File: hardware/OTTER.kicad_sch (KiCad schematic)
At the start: 0 parts

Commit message: added eth symbol
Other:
- added sheet Ethernet (Ethernet.kicad_sch)
- title: (none) -> OTTER Board
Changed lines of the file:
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@@
 	(generator_version "10.0")
 	(paper "A4")
+	(title_block
+		(title "OTTER Board")
+		(date "2026-08-11")
+		(rev "A")
+	)
+	(sheet
+		(at 35.56 29.21)
+		(size 85.09 41.91)
+		(exclude_from_sim no)
+		(in_bom yes)
+		(on_board yes)
+		(dnp no)
+		(fields_autoplaced yes)
+		(stroke
+			(width 0.1524)
+			(type solid)
+		)
+		(fill
+			(color 0 0 0 0)
+		)
+		(property "Sheetname" "Ethernet"
+			(at 35.56 28.4984 0)
+			(show_name no)
+			(do_not_autoplace no)
+			(effects
+				(font
+					(size 1.27 1.27)
+				)
+				(justify left bottom)
+			)
+		)
+		(property "Sheetfile" "Ethernet.kicad_sch"
+			(at 35.56 71.7046 0)
+			(show_name no)
+			(do_not_autoplace no)
+			(effects
+				(font
+					(size 1.27 1.27)
+				)
+				(justify left top)
+			)
+		)
+		(instances
+			(project "OTTER"
+				(path "/db2a353b-4a3a-4ce7-8df7-bc33bc3b7cc7"
+					(page "2")
+				)
+			)
+		)
+	)
 	(sheet_instances
 		(path "/"

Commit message: poop
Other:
- added sheet DDRAM (DDRAM.kicad_sch)
- added sheet HDMI (HDMI.kicad_sch)
- added sheet Periphs (Periphs.kicad_sch)
- added sheet Power (Power.kicad_sch)
- added sheet USB (USB.kicad_sch)
- added sheet ZED (ZED.kicad_sch)
- note added: "+ more bs to come"

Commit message: poop
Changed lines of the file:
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@@
 	(text "+ more bs to come"
 		(exclude_from_sim no)
-		(at 105.664 151.384 0)
+		(at 148.844 154.178 0)
 		(effects
 			(font

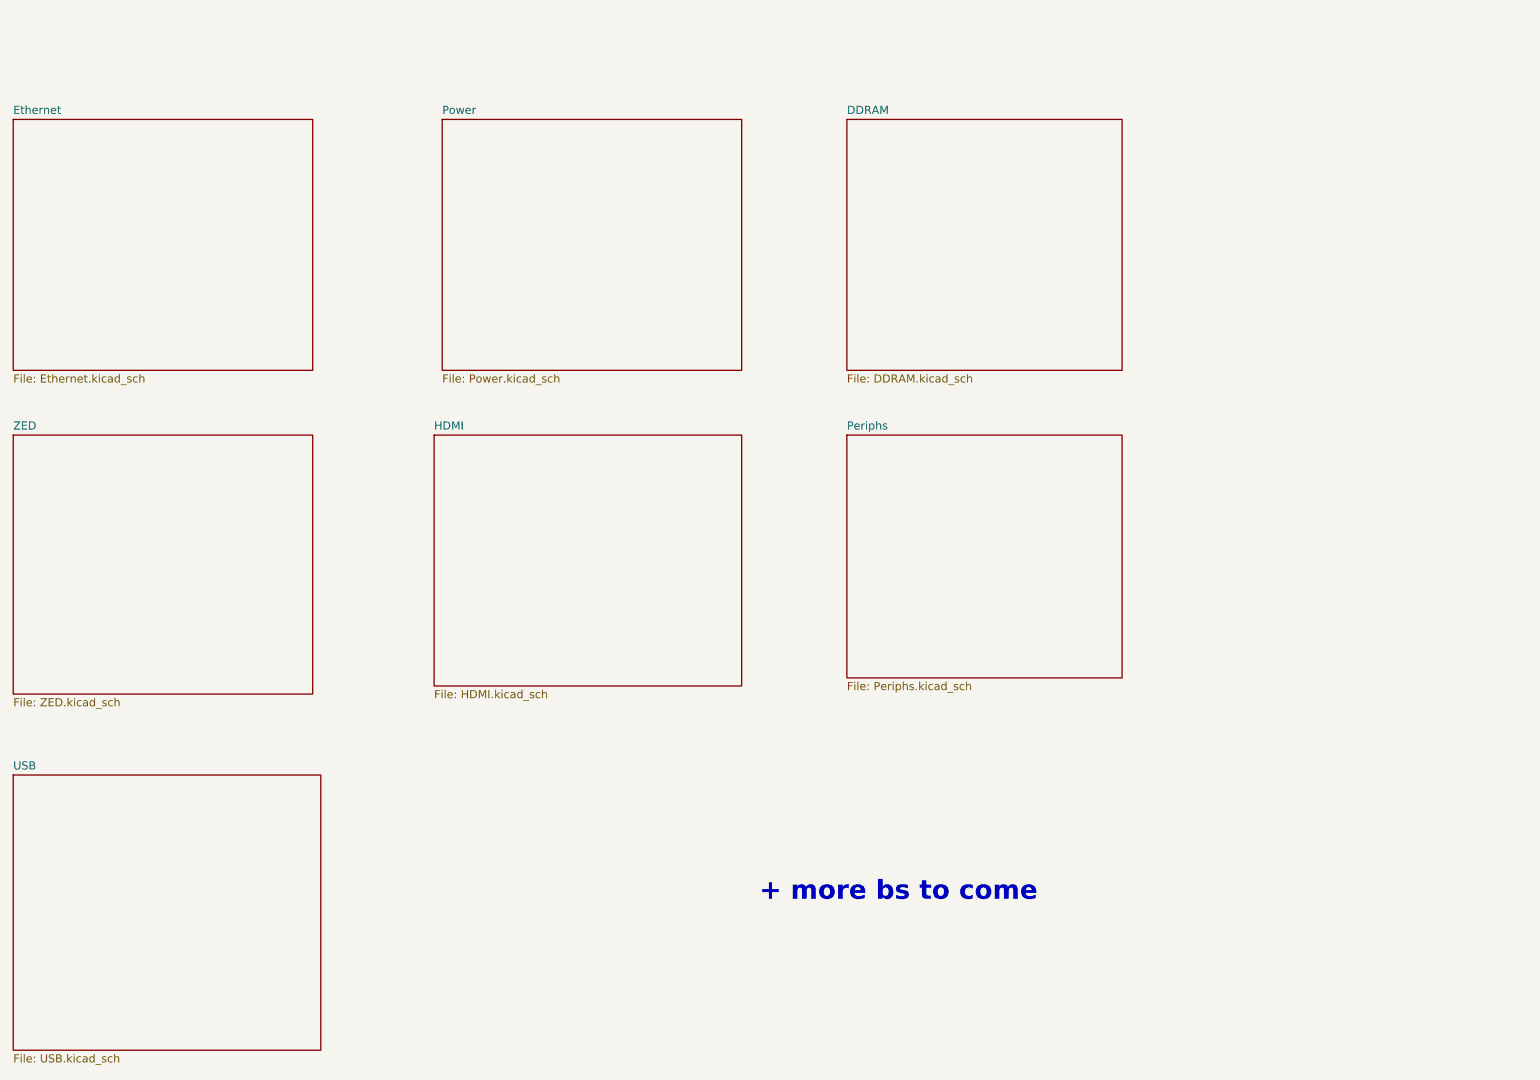
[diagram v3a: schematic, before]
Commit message: finished ethernet
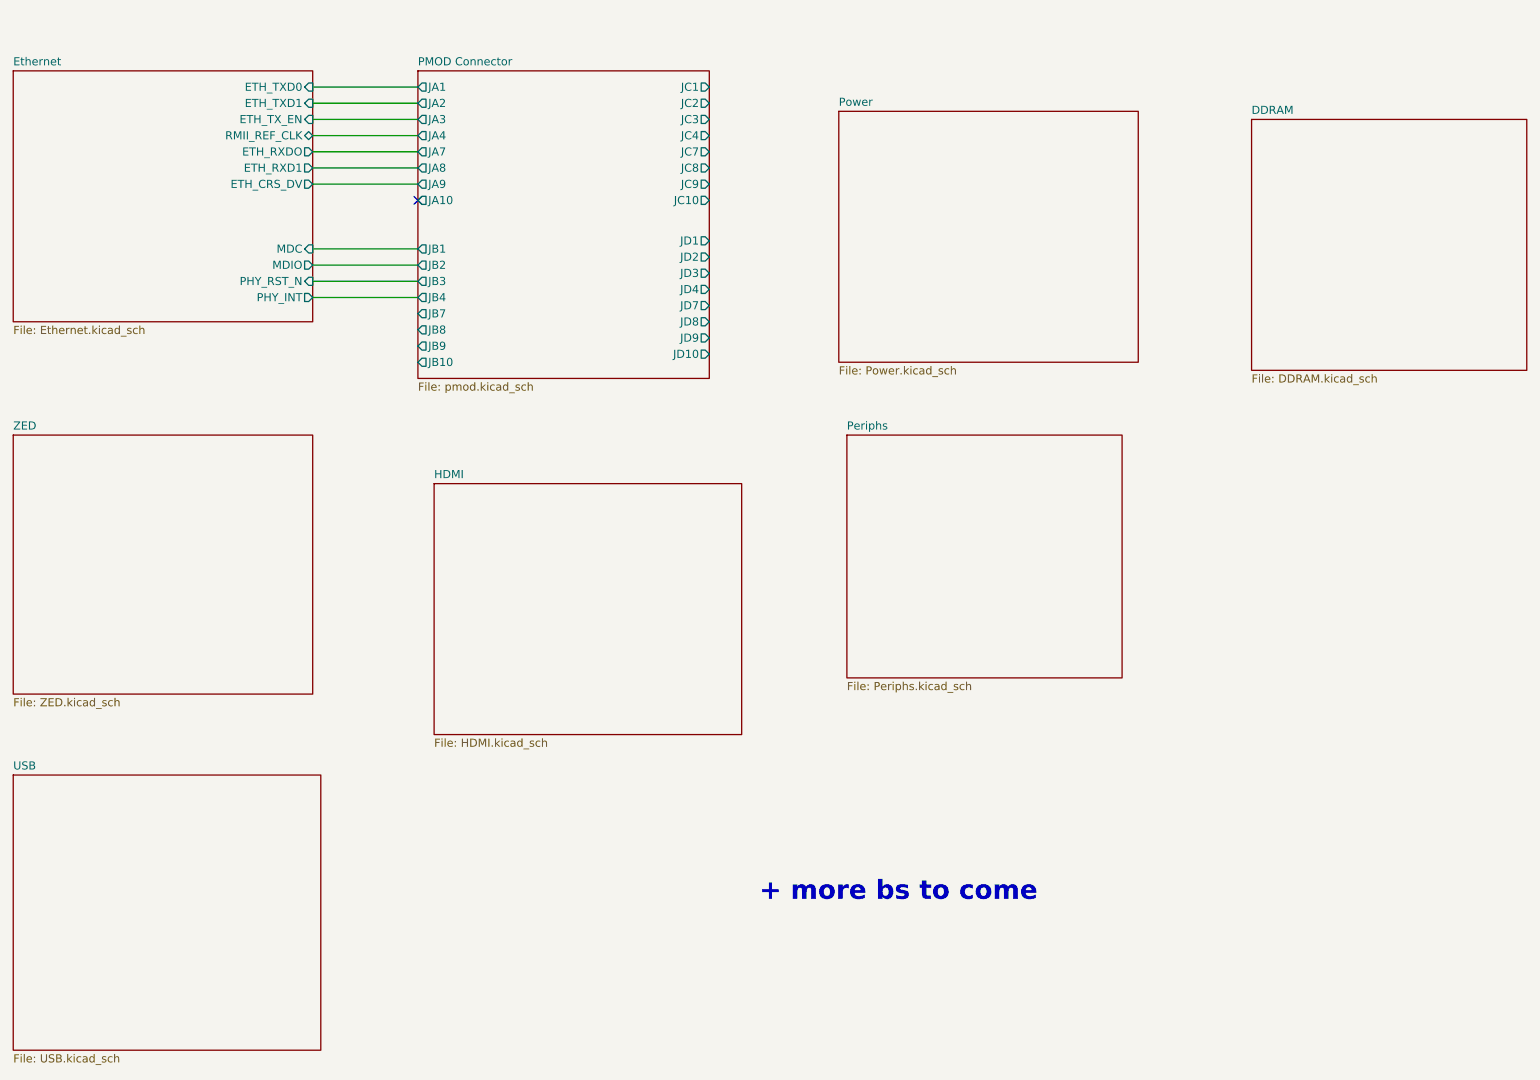
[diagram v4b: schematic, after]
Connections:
- no-connect marks 0 -> 1
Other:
- added sheet PMOD Connector (pmod.kicad_sch)
- sheet Ethernet ports: added ETH_CRS_DV, ETH_RXD1, ETH_RXDO, ETH_TXD0, ETH_TXD1, ETH_TX_EN, MDC, MDIO, PHY_INT, PHY_RST_N, RMII_REF_CLK; removed none

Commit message: added can spi
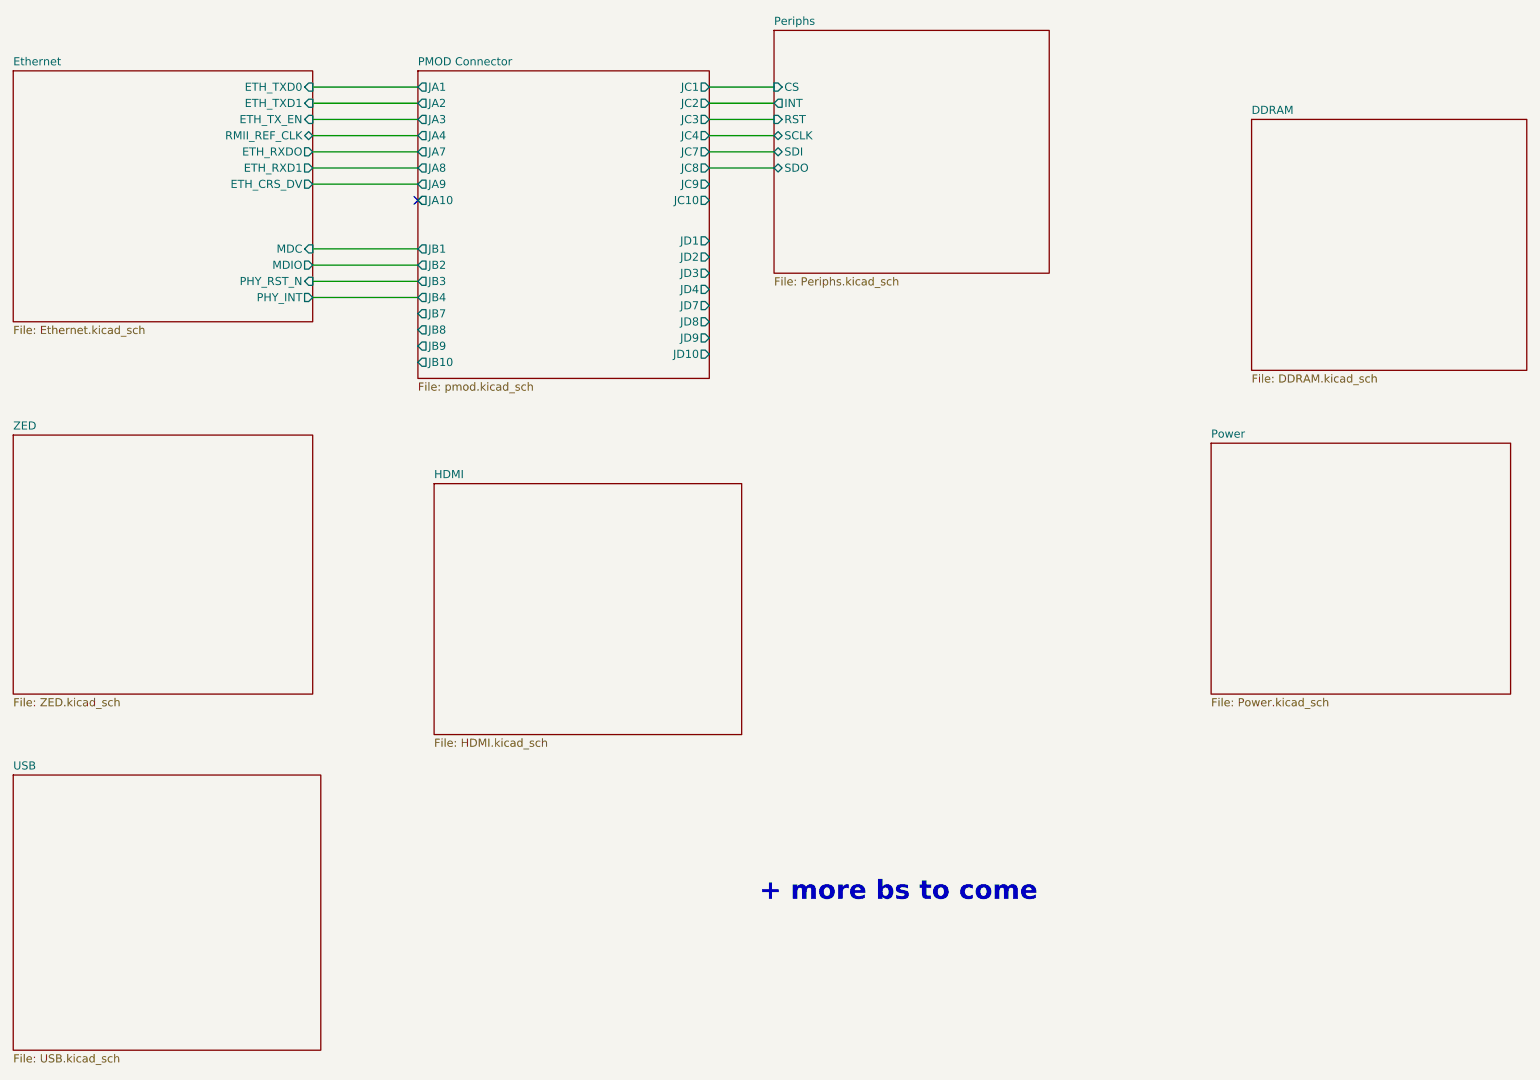
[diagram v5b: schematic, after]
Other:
- sheet Periphs ports: added CS, INT, RST, SCLK, SDI, SDO; removed none
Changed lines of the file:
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@@
+	(wire
+		(pts
+			(xy 140.97 35.56) (xy 151.13 35.56)
+		)
+		(stroke
+			(width 0)
+			(type default)
+		)
+	)
 	(wire
 		(pts
@@
 	(wire
 		(pts
+			(xy 140.97 30.48) (xy 151.13 30.48)
+		)
+		(stroke
+			(width 0)
+			(type default)
+		)
+	)
+	(wire
+		(pts
 			(xy 78.74 38.1) (xy 95.25 38.1)
 		)
@@
 	(wire
 		(pts
+			(xy 140.97 27.94) (xy 151.13 27.94)
+		)
+		(stroke
+			(width 0)
+			(type default)
+		)
+	)
+	(wire
+		(pts
 			(xy 78.74 60.96) (xy 95.25 60.96)
 		)
@@
 	(wire
 		(pts
+			(xy 140.97 38.1) (xy 151.13 38.1)
+		)
+		(stroke
+			(width 0)
+			(type default)
+		)
+	)
+	(wire
+		(pts
 			(xy 78.74 27.94) (xy 95.25 27.94)
 		)
@@
 		(pts
 			(xy 78.74 55.88) (xy 95.25 55.88)
+		)
+		(stroke
+			(width 0)
+			(type default)
+		)
+	)
+	(wire
+		(pts
+			(xy 140.97 40.64) (xy 151.13 40.64)
+		)
+		(stroke
+			(width 0)
+			(type default)
+		)
+	)
+	(wire
+		(pts
+			(xy 140.97 33.02) (xy 151.13 33.02)
 		)
 		(stroke
@@
 	)
 	(sheet
-		(at 161.29 31.75)
+		(at 219.71 83.82)
 		(size 46.99 39.37)
 		(exclude_from_sim no)
@@
 		)
 		(property "Sheetname" "Power"
-			(at 161.29 31.0384 0)
+			(at 219.71 83.1084 0)
 			(show_name no)
 			(do_not_autoplace no)
@@
 		)
 		(property "Sheetfile" "Power.kicad_sch"
-			(at 161.29 71.7046 0)
+			(at 219.71 123.7746 0)
 			(show_name no)
 			(do_not_autoplace no)
@@
 	)
 	(sheet
-		(at 162.56 82.55)
+		(at 151.13 19.05)
 		(size 43.18 38.1)
 		(exclude_from_sim no)
@@
 		)
 		(property "Sheetname" "Periphs"
-			(at 162.56 81.8384 0)
+			(at 151.13 18.3384 0)
 			(show_name no)
 			(do_not_autoplace no)
@@
 		)
 		(property "Sheetfile" "Periphs.kicad_sch"
-			(at 162.56 121.2346 0)
+			(at 151.13 57.7346 0)
 			(show_name no)
 			(do_not_autoplace no)
@@
 			)
 		)
+		(pin "CS" input
+			(at 151.13 27.94 180)
+			(effects
+				(font
+					(size 1.27 1.27)
+				)
+				(justify left)
+			)
+		)
+		(pin "INT" output
+			(at 151.13 30.48 180)
+			(effects
+				(font
+					(size 1.27 1.27)
+				)
+				(justify left)
+			)
+		)
+		(pin "RST" input
+			(at 151.13 33.02 180)
+			(effects
+				(font
+					(size 1.27 1.27)
+				)
+				(justify left)
+			)
+		)
+		(pin "SCLK" bidirectional
+			(at 151.13 35.56 180)
+			(effects
+				(font
+					(size 1.27 1.27)
+				)
+				(justify left)
+			)
+		)
+		(pin "SDI" bidirectional
+			(at 151.13 38.1 180)
+			(effects
+				(font
+					(size 1.27 1.27)
+				)
+				(justify left)
+			)
+		)
+		(pin "SDO" bidirectional
+			(at 151.13 40.64 180)
+			(effects
+				(font
+					(size 1.27 1.27)
+				)
+				(justify left)
+			)
+		)

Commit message: some changes`
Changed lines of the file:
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@@
-	(wire
-		(pts
-			(xy 140.97 35.56) (xy 151.13 35.56)
-		)
-		(stroke
-			(width 0)
-			(type default)
-		)
-	)
 	(wire
 		(pts
@@
 	(wire
 		(pts
+			(xy 140.97 40.64) (xy 157.48 40.64)
+		)
+		(stroke
+			(width 0)
+			(type default)
+		)
+	)
+	(wire
+		(pts
+			(xy 140.97 33.02) (xy 157.48 33.02)
+		)
+		(stroke
+			(width 0)
+			(type default)
+		)
+	)
+	(wire
+		(pts
 			(xy 78.74 40.64) (xy 95.25 40.64)
 		)
@@
 	(wire
 		(pts
-			(xy 140.97 30.48) (xy 151.13 30.48)
-		)
-		(stroke
-			(width 0)
-			(type default)
-		)
-	)
-	(wire
-		(pts
 			(xy 78.74 38.1) (xy 95.25 38.1)
 		)
@@
 	(wire
 		(pts
+			(xy 140.97 30.48) (xy 157.48 30.48)
+		)
+		(stroke
+			(width 0)
+			(type default)
+		)
+	)
+	(wire
+		(pts
 			(xy 78.74 35.56) (xy 95.25 35.56)
 		)
@@
 	(wire
 		(pts
-			(xy 140.97 27.94) (xy 151.13 27.94)
-		)
-		(stroke
-			(width 0)
-			(type default)
-		)
-	)
-	(wire
-		(pts
 			(xy 78.74 60.96) (xy 95.25 60.96)
 		)
@@
 	(wire
 		(pts
-			(xy 140.97 38.1) (xy 151.13 38.1)
+			(xy 140.97 38.1) (xy 157.48 38.1)
+		)
+		(stroke
+			(width 0)
+			(type default)
+		)
+	)
+	(wire
+		(pts
+			(xy 140.97 27.94) (xy 157.48 27.94)
 		)
 		(stroke
@@
 	(wire
 		(pts
-			(xy 140.97 40.64) (xy 151.13 40.64)
-		)
-		(stroke
-			(width 0)
-			(type default)
-		)
-	)
-	(wire
-		(pts
-			(xy 140.97 33.02) (xy 151.13 33.02)
+			(xy 140.97 35.56) (xy 157.48 35.56)
 		)
 		(stroke
@@
 	)
 	(sheet
-		(at 151.13 19.05)
+		(at 157.48 25.4)
 		(size 43.18 38.1)
 		(exclude_from_sim no)
@@
 		)
 		(property "Sheetname" "Periphs"
-			(at 151.13 18.3384 0)
+			(at 157.48 24.6884 0)
 			(show_name no)
 			(do_not_autoplace no)
@@
 		)
 		(property "Sheetfile" "Periphs.kicad_sch"
-			(at 151.13 57.7346 0)
+			(at 157.48 64.0846 0)
 			(show_name no)
 			(do_not_autoplace no)
@@
 		)
 		(pin "CS" input
-			(at 151.13 27.94 180)
+			(at 157.48 27.94 180)
 			(effects
 				(font
@@
 		)
 		(pin "INT" output
-			(at 151.13 30.48 180)
+			(at 157.48 30.48 180)
 			(effects
 				(font
@@
 		)
 		(pin "RST" input
-			(at 151.13 33.02 180)
+			(at 157.48 33.02 180)
 			(effects
 				(font
@@
 		)
 		(pin "SCLK" bidirectional
-			(at 151.13 35.56 180)
+			(at 157.48 35.56 180)
 			(effects
 				(font
@@
 		)
 		(pin "SDI" bidirectional
-			(at 151.13 38.1 180)
+			(at 157.48 38.1 180)
 			(effects
 				(font
@@
 		)
 		(pin "SDO" bidirectional
-			(at 151.13 40.64 180)
-			(effects
-				(font
+			(at 157.48 40.64 180)
+			(effects
+				(font

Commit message: fix
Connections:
- no-connect marks 1 -> 0

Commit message: matthew review or get touched
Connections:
- no-connect marks 0 -> 15
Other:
- sheet PMOD Connector ports: added none; removed JA4
- sheet Periphs ports: added none; removed INT
